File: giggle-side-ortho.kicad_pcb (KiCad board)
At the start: 2 copper layers, 97.5 x 97 mm, 42 parts, among them J1 CONN_05X2SHD, J2 CONN_05X2SHD

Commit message: 4x4 for main.
because why not?
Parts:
- moved J1 9.99 mm to (35.0, 47.1)
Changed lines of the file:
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@@
       (outputdirectory "giggle-side-gbr/"))
   )
-  (gr_text "giggle giggle giggle giggle giggle giggle" (at 78 37) (layer Front)
+  (gr_text "giggle giggle giggle giggle giggle giggle" (at 78 37) (layer F.SilkS)
     (effects (font (size 2.032 1.524) (thickness 0.3048)))
   )
@@
 (net 69 N-diode-50)
 (net 70 N-diode-51)
+(net 71 N-diode-52)
+(net 72 N-diode-53)
+(net 73 N-diode-54)
+(net 74 N-diode-55)
 (net_class
  Default
@@
  (add_net N-diode-49)
  (add_net N-diode-50)
- (add_net N-diode-51))
+ (add_net N-diode-51)
+ (add_net N-diode-52)
+ (add_net N-diode-53)
+ (add_net N-diode-54)
+ (add_net N-diode-55))
 (module connector-shrouded (layer F.Cu)
-  (at 40 38.5 270)
+  (at 35 47.15 270)
   (descr "PLATED THROUGH HOLE - 2X5 SHROUDED HEADER")
   (tags "PLATED THROUGH HOLE - 2X5 SHROUDED HEADER")

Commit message: yes.
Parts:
- moved J1 9.99 mm to (40.0, 38.5)
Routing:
- net N-col-0: track 179.2 -> 183.4 mm
- net N-col-4: track 179.8 -> 181.9 mm
- net N-col-1: track 179.3 -> 181.1 mm
- net N-col-2: track 182.1 -> 182.8 mm

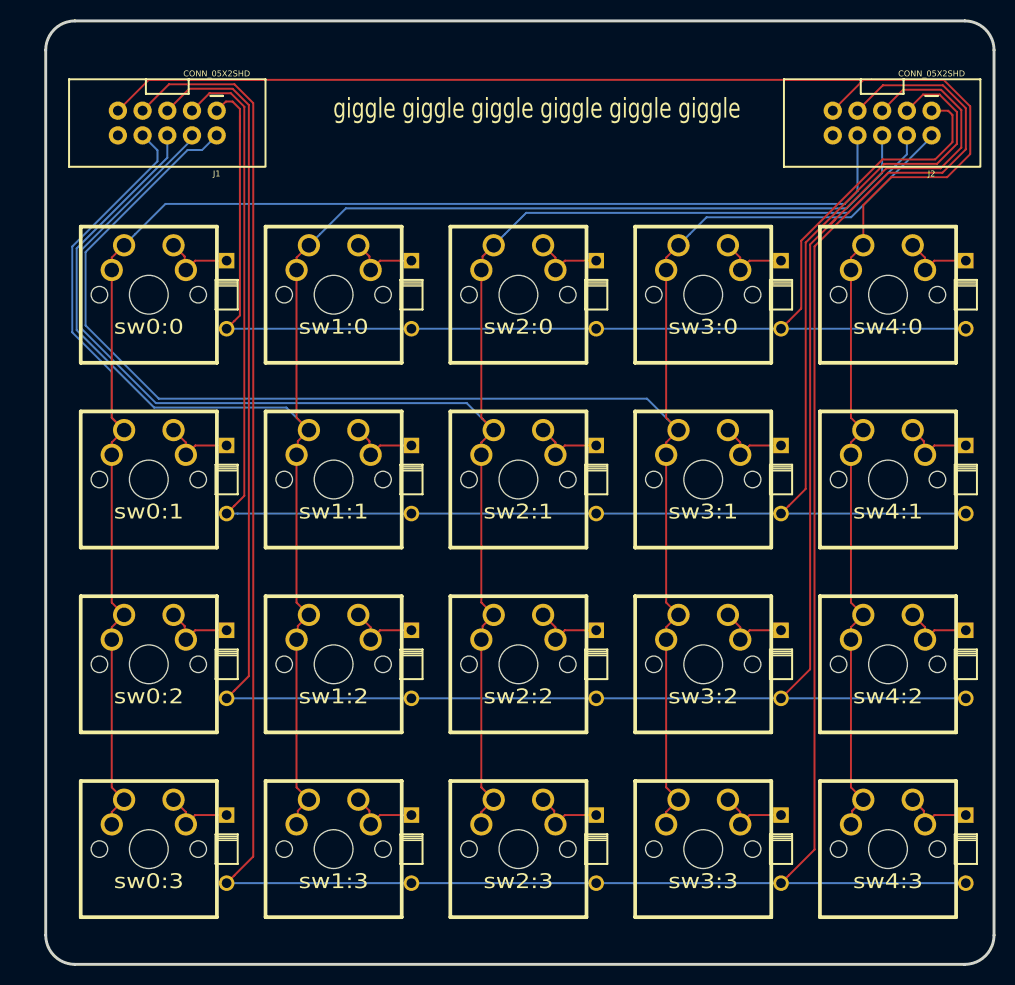
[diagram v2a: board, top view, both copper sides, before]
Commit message: changed switch's footprint and therefore changed the whole traces
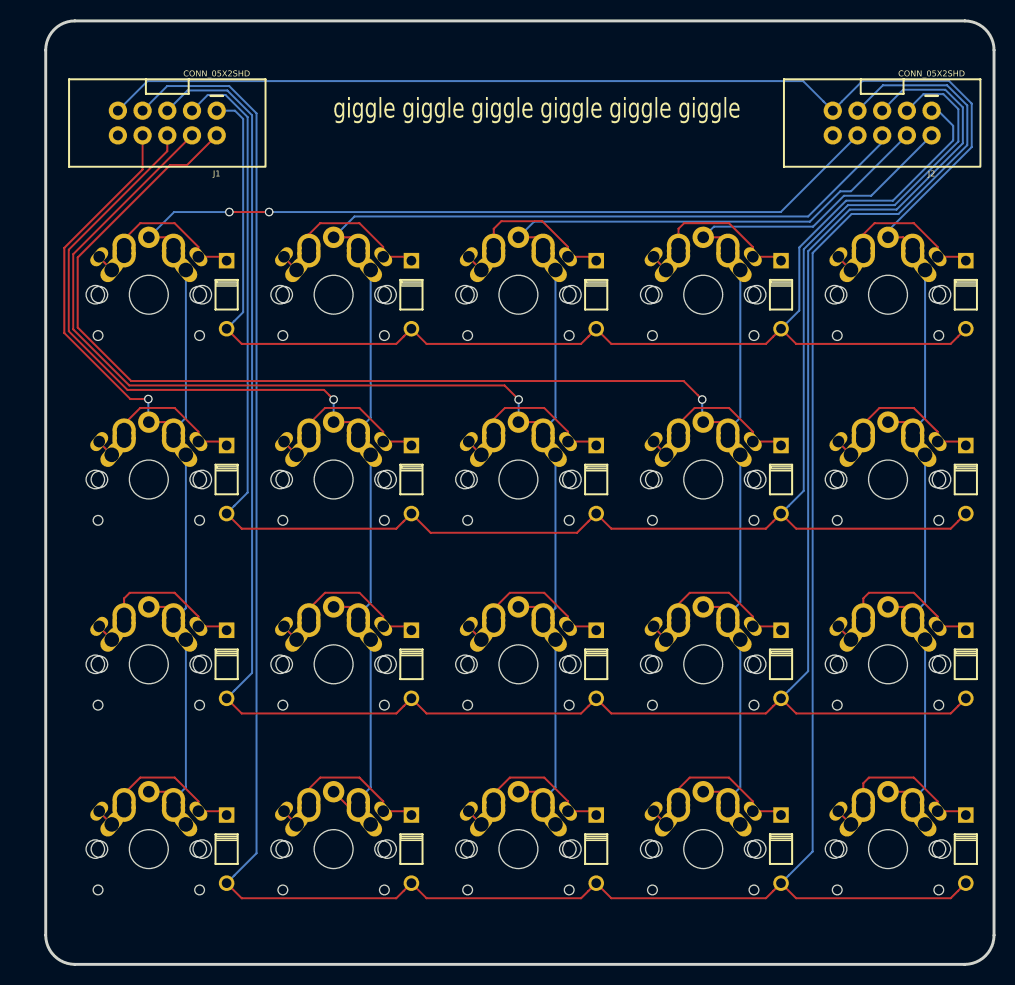
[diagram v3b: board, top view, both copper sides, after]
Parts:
- sw0:0, sw0:1, sw0:2, sw0:3, sw1:0, sw1:1, sw1:2, sw1:3, sw2:0, sw2:1, sw2:2, sw2:3, sw3:0, sw3:1, sw3:2, sw3:3, sw4:0, sw4:1, sw4:2, sw4:3: value (none) -> SW_PUSH; footprint MX_FLIP -> kbd:MX_ALPS_PG1350_noLed
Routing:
- net N-col-11: track 7.65 -> 19.5 mm
- net N-diode-6: track 7.65 -> 19.3 mm
- net N-diode-5: track 7.65 -> 19.3 mm
- net N-diode-0: track 7.65 -> 19.3 mm
- net N-diode-7: track 7.65 -> 19.3 mm
- net N-diode-9: track 7.65 -> 19.0 mm
- net N-diode-10: track 7.65 -> 19.0 mm
- net N-diode-4: track 7.65 -> 19.0 mm
- net N-diode-1: track 7.65 -> 19.0 mm
- net N-diode-8: track 7.65 -> 19.0 mm
- net N-col-6: track 7.65 -> 19.0 mm
- net N-diode-2: track 7.65 -> 19.0 mm
- net N-col-8: track 7.65 -> 19.0 mm
- net N-col-5: track 7.65 -> 19.0 mm
- net N-col-10: track 7.65 -> 19.0 mm
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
